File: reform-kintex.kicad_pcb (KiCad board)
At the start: 8 copper layers, 68 x 67.8 mm, 146 parts, among them J1 Conn_01x33, U1 MNT Reform 2.0 SoM Socket, U10 W25Q128JVS, U11 TPS62823DLC, U12 TPS62823DLC, U13 TPS62823DLC, U14 TPS62823DLC, U15 TPS62823DLC, U16 TPS62823DLC, U2 XC7K160T-FFG676, U3 IS43TR16512B-125KBLI, U4 IS43TR16512B-125KBLI, U5 TPS51200DRC, U6 KSZ9031RNXCA, U7 TUSB1310ZAY, U8 TC358778XBG, U9 SiI9022A

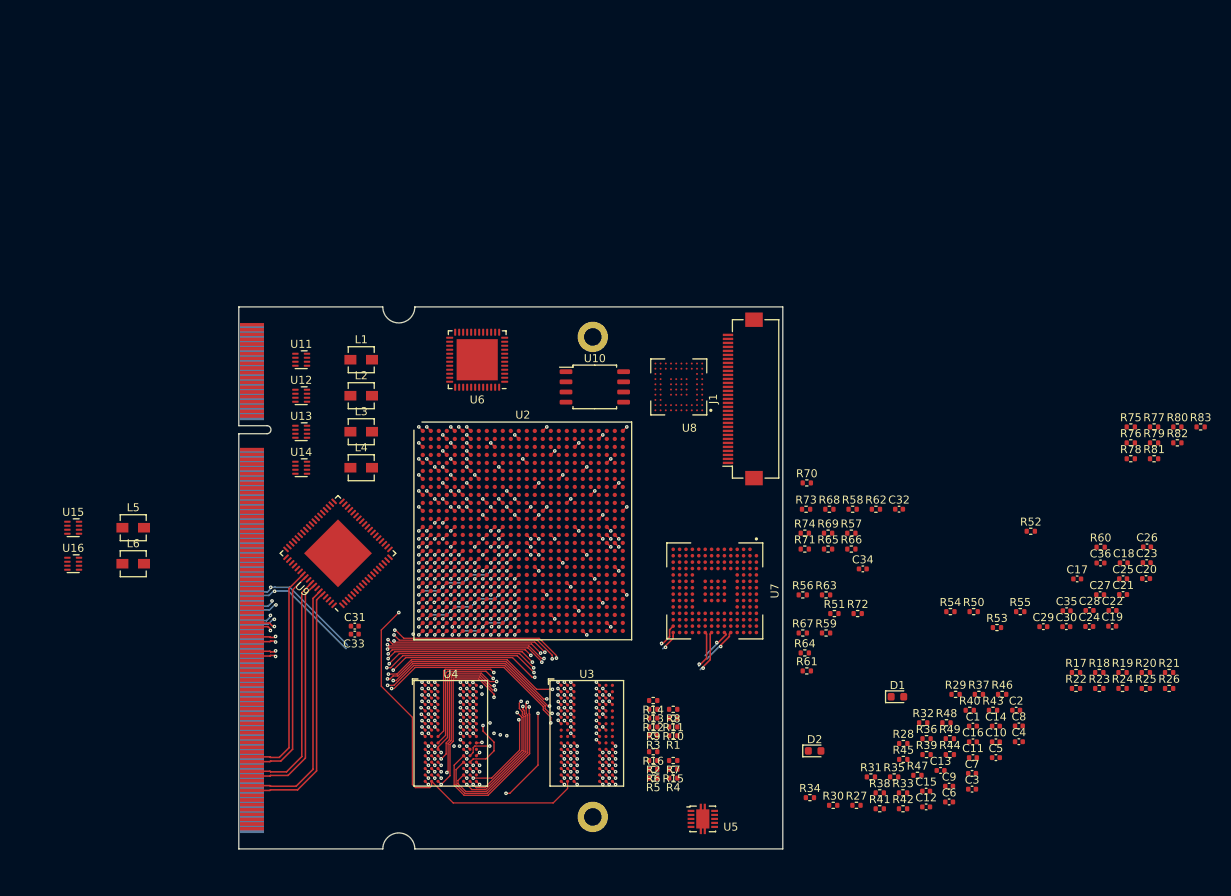
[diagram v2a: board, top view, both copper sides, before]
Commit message: ram bus termination
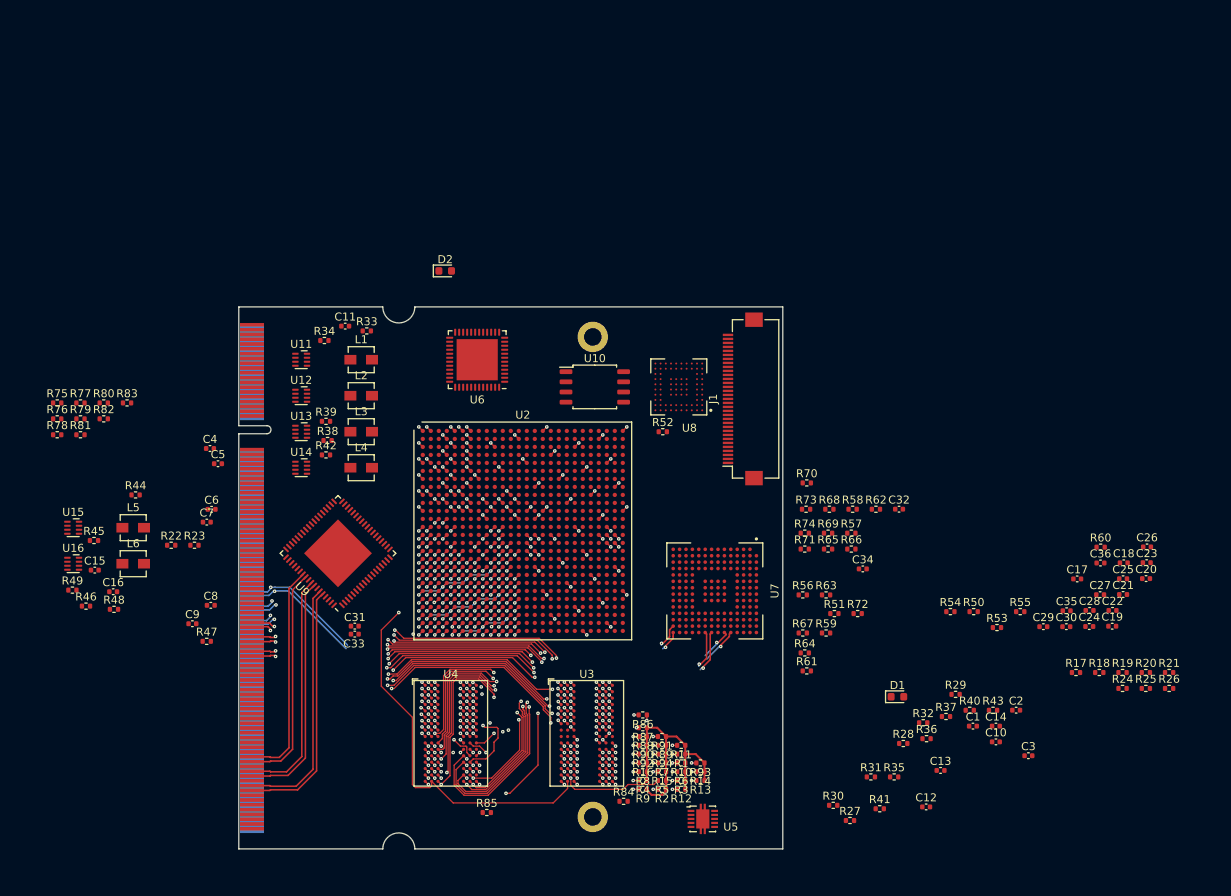
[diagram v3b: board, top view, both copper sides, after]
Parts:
- added R84: 240 1%, Resistor_SMD:R_0402_1005Metric, F.Cu at (148.1, 161.8)
- added R85: 240 1%, Resistor_SMD:R_0402_1005Metric, F.Cu at (131.0, 163.2)
- added R86: 80.6, Resistor_SMD:R_0402_1005Metric, F.Cu at (150.5, 151.0)
- added R87: 40, Resistor_SMD:R_0402_1005Metric, F.Cu at (150.5, 152.6)
- added R88: 40, Resistor_SMD:R_0402_1005Metric, F.Cu at (150.5, 153.7)
- added R89: 40, Resistor_SMD:R_0402_1005Metric, F.Cu at (152.9, 154.8)
- added R90: 40, Resistor_SMD:R_0402_1005Metric, F.Cu at (150.5, 154.8)
- added R91: 40, Resistor_SMD:R_0402_1005Metric, F.Cu at (152.9, 153.7)
- added R92: 40, Resistor_SMD:R_0402_1005Metric, F.Cu at (150.5, 155.9)
- added R93: 40, Resistor_SMD:R_0402_1005Metric, F.Cu at (157.7, 157.0)
- added R94: 40, Resistor_SMD:R_0402_1005Metric, F.Cu at (152.9, 155.9)
- moved R75 134.2 mm to (77.3, 112.0)
- moved R76 134.2 mm to (77.3, 114.0)
- moved R77 134.2 mm to (80.2, 112.0)
- moved R78 134.2 mm to (77.3, 116.0)
- moved R79 134.2 mm to (80.2, 114.0)
- moved R80 134.2 mm to (83.1, 112.0)
- moved R81 134.2 mm to (80.2, 116.0)
- moved R82 134.2 mm to (83.1, 114.0)
- moved R83 134.2 mm to (86.0, 112.0)
- moved R46 115.0 mm to (80.9, 137.4)
- moved R22 114.5 mm to (91.5, 129.8)
- moved R23 114.5 mm to (94.5, 129.8)
- moved R49 111.2 mm to (79.2, 135.4)
- moved C16 109.1 mm to (84.3, 135.6)
- moved C4 107.5 mm to (96.4, 117.7)
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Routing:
- net RAM_RAS#: track 44.7 -> 86.8 mm, vias 3 -> 5
- net Vtt: track 0.00 -> 32.6 mm
- net RAM_A7: track 36.3 -> 64.3 mm
- net RAM_CK-: track 32.7 -> 58.6 mm, vias 3 -> 4
- net RAM_CK+: track 30.3 -> 54.2 mm, vias 3 -> 4
- net RAM_A5: track 47.7 -> 61.4 mm, vias 4 -> 5
- net RAM_BA1: track 43.2 -> 56.0 mm, vias 4 -> 5
- net RAM_A10: track 43.1 -> 55.1 mm
- net RAM_WE#: track 45.4 -> 57.0 mm, vias 4 -> 5
- net RAM_A6: track 56.6 -> 68.0 mm, vias 4 -> 5
- net RAM_A3: track 39.6 -> 50.8 mm, vias 3 -> 4
- net RAM_BA0: track 42.2 -> 53.3 mm, vias 4 -> 5
- net RAM_A4: track 48.0 -> 59.0 mm, vias 4 -> 5
- net RAM_A2: track 49.2 -> 59.9 mm, vias 3 -> 4
- net RAM_BA2: track 48.6 -> 59.3 mm, vias 4 -> 5
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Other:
- rule pad_to_mask_clearance: 0.05 -> 0

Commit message: DSI and some USB routing
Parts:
- C31, C33: moved to B.Cu
- moved R21 127.4 mm to (91.4, 120.4)
- moved R20 125.4 mm to (88.3, 137.4)
- moved C1 118.6 mm to (82.8, 105.6)
- moved R29 118.6 mm to (80.6, 101.6)
- moved R37 118.6 mm to (79.4, 104.4)
- moved R40 118.6 mm to (82.4, 103.6)
- moved R43 118.6 mm to (85.3, 103.6)
- moved C10 118.6 mm to (85.6, 107.6)
- moved C14 118.6 mm to (85.6, 105.6)
- moved C2 118.6 mm to (88.2, 103.6)
- moved C3 118.6 mm to (89.7, 109.3)
- moved R17 114.1 mm to (91.2, 133.8)
- moved R18 114.1 mm to (94.1, 133.8)
- moved R19 114.1 mm to (97.0, 133.8)
- moved R25 104.5 mm to (124.4, 92.8)
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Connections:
- U2 pad AA14: DISP2_RGB11 -> DISP2_RGB6
- U2 pad AA15: DISP2_RGB10 -> DISP2_DE
- U2 pad AA17: DISP2_RGB3 -> DISP2_RGB17
- U2 pad AA18: DISP2_RGB2 -> DISP2_RGB19
- U2 pad AB14: DISP2_RGB5 -> DISP2_RGB16
- U2 pad AB15: DISP2_RGB4 -> DISP2_HS
- U2 pad AB16: DISP2_RGB1 -> DISP2_VS
- U2 pad AB17: DISP2_HS -> DISP2_RGB21
- U2 pad AC14: DISP2_RGB9 -> DISP2_RGB15
- U2 pad AC16: DISP2_RGB0 -> DISP2_RGB12
- U2 pad AC17: DISP2_VS -> DISP2_RGB14
- U2 pad AD14: DISP2_RGB8 -> DISP2_RGB13
- U2 pad AD15: DISP2_RGB17 -> DISP2_RGB8
- U2 pad AD16: DISP2_RGB13 -> DISP2_RGB10
- U2 pad AD20: DISP2_DE -> DISP2_RGB23
- U2 pad AE15: DISP2_RGB16 -> DISP2_RGB3
- U2 pad AE16: DISP2_RGB12 -> DISP2_RGB2
- U2 pad AE17: DISP2_RGB23 -> DISP2_RGB4
- U2 pad AE18: DISP2_RGB19 -> DISP2_RGB9
- U2 pad AF14: DISP2_RGB21 -> DISP2_RGB1
- U2 pad AF15: DISP2_RGB20 -> DISP2_RGB0
- U2 pad AF17: DISP2_RGB22 -> DISP2_RGB5
- U2 pad AF18: DISP2_RGB18 -> DISP2_RGB7
- U2 pad AF19: DISP2_RGB15 -> DISP2_RGB11
- U2 pad AF20: DISP2_RGB14 -> DISP2_RGB22
- U2 pad Y15: DISP2_RGB7 -> DISP2_RGB18
- U2 pad Y16: DISP2_RGB6 -> DISP2_RGB20
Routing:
- net /RAM/USB1TXN: track 5.34 -> 99.2 mm, vias 1 -> 2
- net /RAM/USB1TXP: track 4.78 -> 97.8 mm, vias 1 -> 2
- net USB1_RX_N: track 7.39 -> 98.5 mm
- net USB1_DN: track 18.4 -> 109.1 mm
- net USB1_RX_P: track 7.20 -> 96.9 mm
- net USB1_DP: track 17.7 -> 106.7 mm
- net DISP2_HS: track 0.00 -> 34.8 mm, vias 0 -> 2
- net DISP2_RGB20: track 0.00 -> 34.6 mm, vias 0 -> 2
- net DISP2_RGB6: track 0.00 -> 33.2 mm, vias 0 -> 2
- net DISP2_DE: track 0.00 -> 33.1 mm, vias 0 -> 2
- net DISP2_VS: track 0.00 -> 32.5 mm, vias 0 -> 2
- net DISP2_PCLK: track 0.00 -> 32.4 mm, vias 0 -> 2
- net DISP2_RGB18: track 0.00 -> 32.2 mm, vias 0 -> 2
- net HDMI_D2+: track 31.5 -> 0.00 mm
- net DISP2_RGB16: track 0.00 -> 31.3 mm, vias 0 -> 2
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
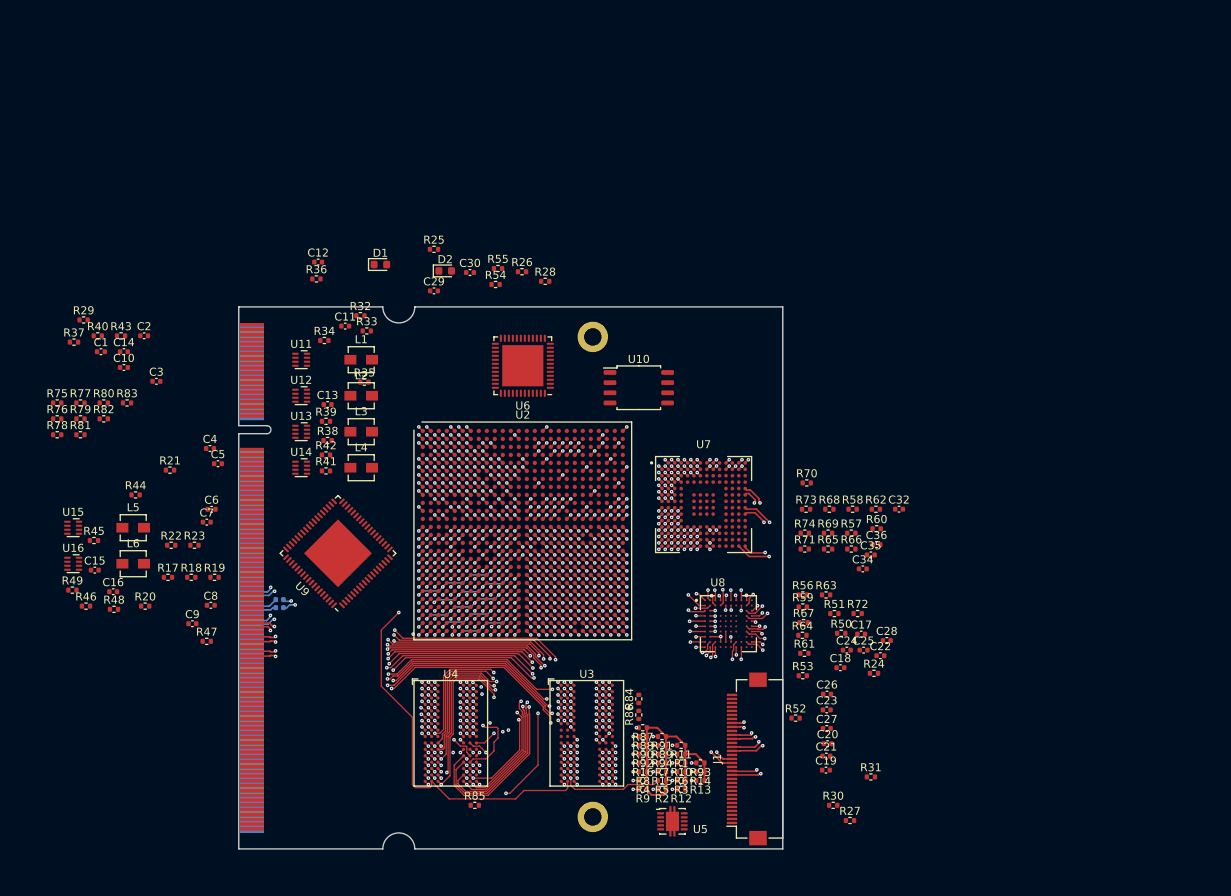
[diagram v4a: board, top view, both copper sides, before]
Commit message: more routing, esp. ethernet
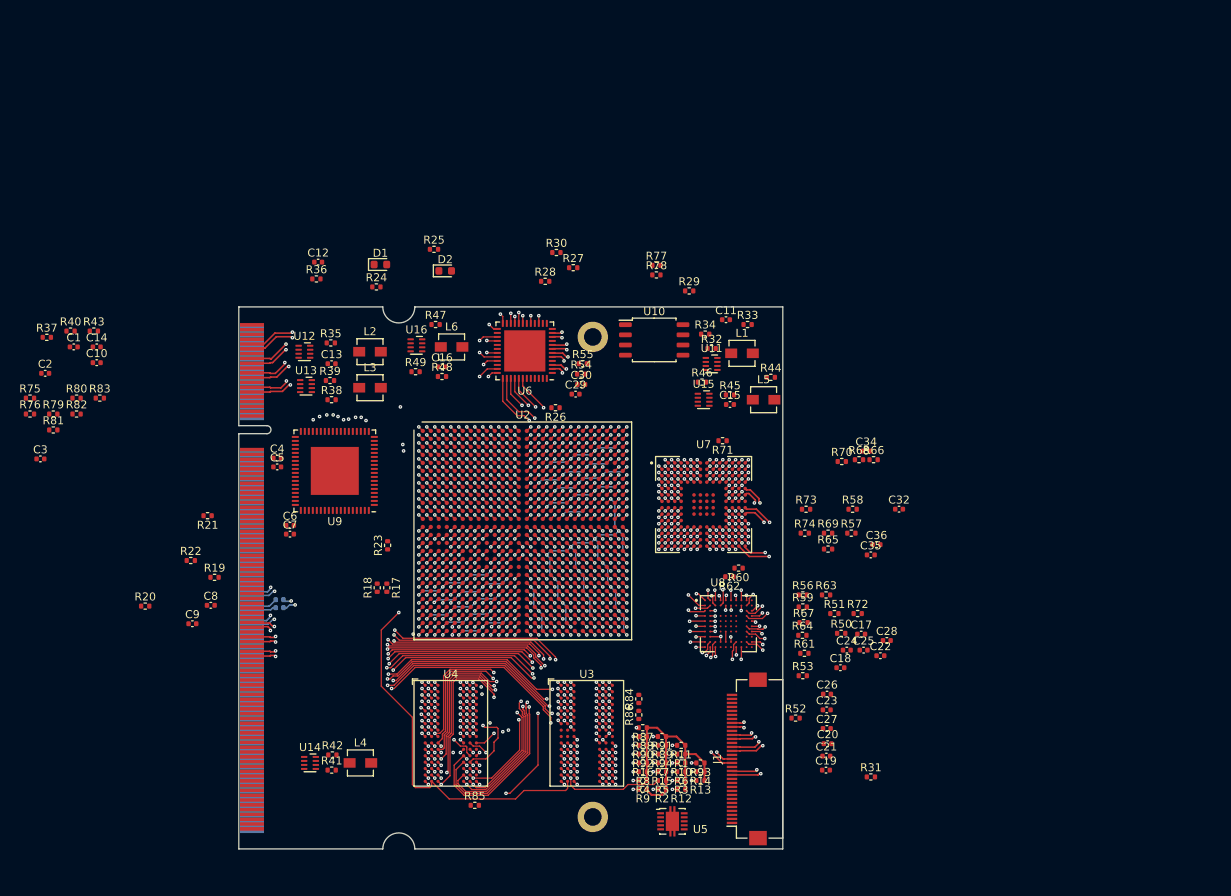
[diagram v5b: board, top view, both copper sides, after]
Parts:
- moved C15 82.1 mm to (161.4, 112.2)
- moved R46 81.9 mm to (157.9, 109.4)
- moved R45 81.6 mm to (161.4, 111.0)
- moved R44 80.7 mm to (166.5, 108.8)
- moved L5 80.4 mm to (165.6, 111.6)
- moved U15 80.4 mm to (158.1, 111.6)
- moved R24 78.8 mm to (117.2, 97.5)
- moved R78 77.5 mm to (152.2, 96.0)
- moved R30 77.3 mm to (139.7, 93.2)
- moved R27 77.3 mm to (141.8, 95.1)
- moved R29 75.8 mm to (156.3, 98.0)
- moved R77 74.0 mm to (152.2, 94.8)
- moved U11 51.3 mm to (159.1, 107.1)
- moved R49 50.8 mm to (122.1, 108.1)
- moved U16 50.8 mm to (122.2, 104.8)
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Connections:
- U2 pad A10: Net-(U2-PadA10) -> SD2_DATA2
- U2 pad A12: Net-(U2-PadA12) -> SD2_CD
- U2 pad A14: Net-(U2-PadA14) -> SD2_DATA0
- U2 pad A15: Net-(U2-PadA15) -> SD2_CMD
- U2 pad A17: SD2_CLK -> Net-(U2-PadA17)
- U2 pad A18: SD2_DATA2 -> Net-(U2-PadA18)
- U2 pad A19: SD2_DATA3 -> Net-(U2-PadA19)
- U2 pad AB21: TUSB_PDOWN1 -> TUSB_ULPI_D2
- U2 pad AC21: TUSB_TX_ELECIDLE -> TUSB_ULPI_D0
- U2 pad AC22: TUSB_PDOWN0 -> TUSB_TX_DATAK1
- U2 pad AD21: TUSB_RX_ELECIDLE -> TUSB_ULPI_D1
- U2 pad AD23: TUSB_PWRPRESENT -> TUSB_TX_D15
- U2 pad AD24: TUSB_PHYRESETN -> TUSB_ULPI_DIR
- U2 pad AD25: TUSB_ULPI_D3 -> TUSB_ENAB
- U2 pad AD26: TUSB_ULPI_STP -> TUSB_PDOWN1
- U2 pad AE21: TUSB_PHY_STATUS -> TUSB_ULPI_NXT
- U2 pad AE22: TUSB_ULPI_D5 -> TUSB_PWRPRESENT
- U2 pad AE23: TUSB_ULPI_D1 -> TUSB_RX_ELECIDLE
- U2 pad AE25: TUSB_ULPI_D4 -> TUSB_RX_D13
- U2 pad AE26: TUSB_ULPI_D0 -> TUSB_RX_D12
- U2 pad AF22: TUSB_ULPI_D6 -> TUSB_ULPI_CLK
- U2 pad AF23: TUSB_ULPI_D2 -> TUSB_RX_D14
- U2 pad AF24: TUSB_ULPI_DIR -> TUSB_RX_D15
- U2 pad AF25: TUSB_ULPI_NXT -> TUSB_RESETN
- U2 pad B10: Net-(U2-PadB10) -> SD2_DATA1
- U2 pad B15: Net-(U2-PadB15) -> SD2_DATA3
- U2 pad B16: SD2_DATA1 -> Net-(U2-PadB16)
- U2 pad B17: SD2_CMD -> Net-(U2-PadB17)
- U2 pad B19: UART2_RX -> Net-(U2-PadB19)
- U2 pad C11: Net-(U2-PadC11) -> SD2_CLK
- U2 pad C16: SD2_DATA0 -> UART2_RX
- U2 pad C19: SD2_CD -> Net-(U2-PadC19)
- U2 pad D18: ETH_TX_CLK -> ETH_RX_CLK
- U2 pad D19: ETH_RX_D1 -> ETH_TX_EN
- U2 pad D20: ETH_RX_D2 -> ETH_RX_D3
- U2 pad E15: ETH_INT_N -> ETH_MDIO
- U2 pad E16: ETH_RST_N -> ETH_INT_N
- U2 pad E17: ETH_TX_D2 -> ETH_MDC
- U2 pad E18: ETH_TX_D3 -> ETH_TX_CLK
- U2 pad F15: ETH_REF_CLK -> ETH_RX_DV
- U2 pad F17: ETH_TX_D1 -> ETH_REF_CLK
- U2 pad F18: ETH_TX_D0 -> ETH_TX_D3
- U2 pad F20: ETH_RX_CLK -> ETH_RX_D2
- U2 pad G17: ETH_TX_EN -> ETH_RST_N
- U2 pad G19: ETH_RX_D3 -> ETH_TX_D2
- U2 pad H17: ETH_RX_DV -> ETH_TX_D1
- U2 pad H18: ETH_RX_D0 -> ETH_TX_D0
- U2 pad J15: ETH_MDIO -> ETH_RX_D0
- U2 pad J16: ETH_MDC -> ETH_RX_D1
- U2 pad K25: TUSB_RX_STAT2 -> TUSB_RX_D11
- U2 pad K26: TUSB_RX_STAT1 -> TUSB_RX_K0
- U2 pad L24: TUSB_RX_D11 -> TUSB_RX_D10
- U2 pad L25: TUSB_RX_D1 -> TUSB_RX_K1
- U2 pad M20: TUSB_RX_D9 -> TUSB_TX_D12
- U2 pad M21: TUSB_RX_D14 -> TUSB_TX_DATAK0
- U2 pad M22: TUSB_RX_D15 -> TUSB_TX_D14
- U2 pad M24: TUSB_RX_D10 -> TUSB_RX_STAT0
- U2 pad M25: TUSB_RX_D0 -> TUSB_RX_D1
- U2 pad M26: TUSB_RX_D5 -> TUSB_RX_D2
- U2 pad N17: TUSB_TX_D9 -> TUSB_RX_STAT1
- U2 pad N18: TUSB_TX_D12 -> TUSB_RX_D8
- U2 pad N19: TUSB_RX_D8 -> TUSB_RX_D6
- U2 pad N23: TUSB_RX_K0 -> TUSB_PDOWN0
- U2 pad N24: TUSB_RX_D3 -> TUSB_TX_ELECIDLE
- U2 pad N26: TUSB_RX_D4 -> TUSB_TX_D10
- U2 pad P16: TUSB_TX_D8 -> TUSB_RX_STAT2
- U2 pad P18: TUSB_TX_DATAK0 -> TUSB_RX_D7
- U2 pad P19: TUSB_RX_D12 -> Net-(U2-PadP19)
- U2 pad P20: TUSB_RX_D13 -> Net-(U2-PadP20)
- U2 pad P23: TUSB_RX_K1 -> TUSB_PHYRESETN
- U2 pad P24: TUSB_RX_D2 -> TUSB_TX_D9
- U2 pad P25: TUSB_RX_D7 -> TUSB_TX_D7
- U2 pad P26: TUSB_RX_VALID -> TUSB_TX_D1
- U2 pad R16: TUSB_TX_D10 -> TUSB_ULPI_D7
- U2 pad R17: TUSB_TX_D11 -> TUSB_TX_D3
- U2 pad R18: TUSB_TX_DATAK1 -> TUSB_RX_D3
- U2 pad R20: TUSB_TX_D1 -> TUSB_RX_D0
- U2 pad R22: Net-(U2-PadR22) -> TUSB_TX_D8
- U2 pad R23: Net-(U2-PadR23) -> TUSB_TX_D6
- U2 pad R25: TUSB_RX_D6 -> TUSB_TX_D0
- U2 pad R26: TUSB_RX_STAT0 -> TUSB_RX_VALID
- U2 pad T17: TUSB_TX_D15 -> TUSB_ULPI_D6
- U2 pad T18: TUSB_TX_D6 -> TUSB_TX_D2
- U2 pad T19: TUSB_TX_D7 -> TUSB_RX_D9
- U2 pad T20: TUSB_TX_D0 -> TUSB_TX_D5
- U2 pad T22: TUSB_TX_D2 -> TUSB_PHY_STATUS
- U2 pad T23: TUSB_TX_D3 -> TUSB_RX_D4
- U2 pad T25: Net-(U2-PadT25) -> TUSB_RX_D5
- U2 pad U17: TUSB_TX_D14 -> TUSB_ULPI_D5
- U2 pad U20: TUSB_TX_D5 -> TUSB_TX_D11
- U2 pad W20: TUSB_ENAB -> TUSB_ULPI_D4
- U2 pad Y20: TUSB_ULPI_D7 -> TUSB_ULPI_D3
- U2 pad Y21: TUSB_RESETN -> TUSB_ULPI_STP
- U2 pad Y22: TUSB_ULPI_CLK -> Net-(U2-PadY22)
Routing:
- net +1V8: track 25.9 -> 93.3 mm, vias 38 -> 51
- net ETH0_B-: track 0.00 -> 42.7 mm, vias 0 -> 2
- net ETH0_A-: track 0.00 -> 42.4 mm, vias 0 -> 2
- net DISP1_HS: track 0.71 -> 42.9 mm, vias 1 -> 2
- net ETH0_C-: track 0.00 -> 42.1 mm, vias 0 -> 2
- net ETH0_C+: track 0.00 -> 42.0 mm, vias 0 -> 2
- net ETH0_B+: track 0.00 -> 41.8 mm, vias 0 -> 2
- net ETH0_A+: track 0.00 -> 41.5 mm, vias 0 -> 2
- net ETH0_D-: track 0.00 -> 40.8 mm, vias 0 -> 2
- net ETH0_D+: track 0.00 -> 40.8 mm, vias 0 -> 2
- net DISP1_VS: track 0.00 -> 39.8 mm, vias 0 -> 2
- net +3V3: track 4.95 -> 38.4 mm, vias 7 -> 16
- net TUSB_RX_D5: track 1.27 -> 34.6 mm
- net ETH_TX_D0: track 0.00 -> 31.5 mm, vias 0 -> 2
- net ETH_TX_D1: track 0.00 -> 31.1 mm, vias 0 -> 2
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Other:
- board text added: "dnp"
